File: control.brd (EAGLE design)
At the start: 146.1 x 33.7 mm, 4 parts, among them J1 1-2328702-0, U2 ESP32-DEVKITC-32D

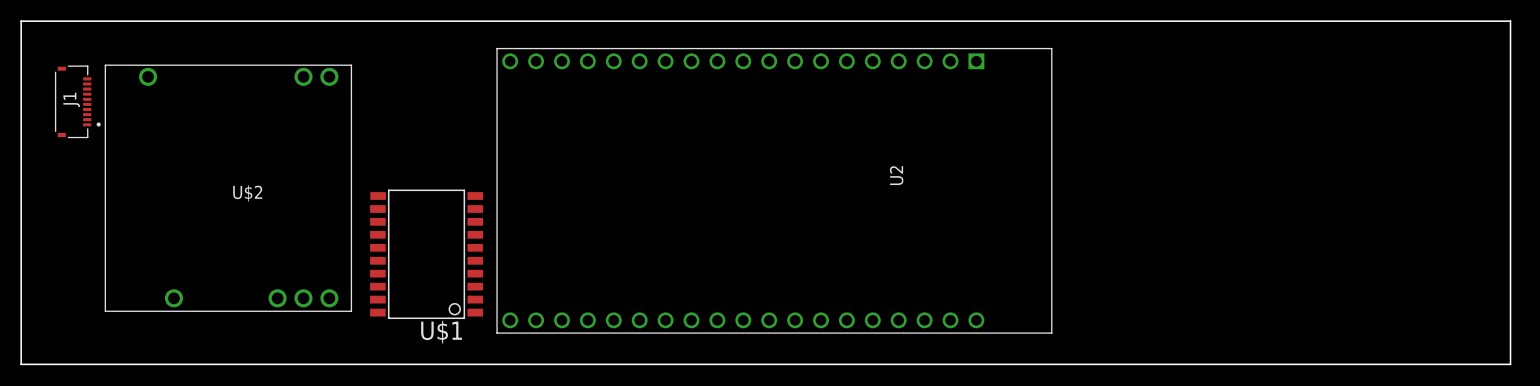
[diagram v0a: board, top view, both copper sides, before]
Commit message: lamp board finished, working on control
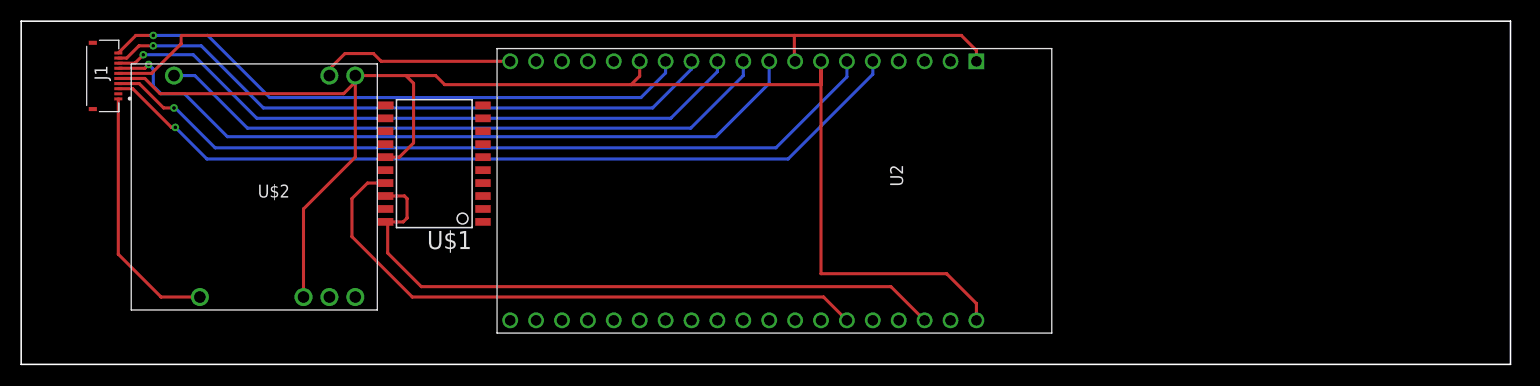
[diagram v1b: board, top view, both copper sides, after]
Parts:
- moved U$1 8.92 mm to (40.5, 19.7)
- moved J1 3.97 mm to (9.53, 26.0)
- moved U$2 2.54 mm to (34.9, 29.5)
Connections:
- removed net EXT_5V: U2.19
- removed net GND1: U2.14
- removed net GND3: U2.20
- new net 5V: U$2.VIN, U2.19
- new net BL: J1.8, U2.11
- new net CLK: J1.4, U2.6
- new net EN: U$2.ENABLE, U2.10
- new net GND: J1.5, U$1.GND, U$2.GND@1, U$2.GND@2, U2.14, U2.20, U2.7
- new net HV: J1.1, U$2.VOUT
- new net IN: J1.9, U2.12
- new net LE: J1.7, U2.9
- new net OUT: J1.10, U2.13
- new net POL: J1.3, U2.5
- new net SCL: U$1.SCL@0, U$1.SCL@1, U2.22
- new net SDA: U$1.SDA, U2.25
- net 3V3: now also J1.6, U2.8
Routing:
- net GND: track 0.00 -> 148.3 mm
- net 3V3: track 0.00 -> 90.4 mm
- net POL: track 0.00 -> 81.6 mm, vias 0 -> 1
- net CLK: track 0.00 -> 78.5 mm, vias 0 -> 1
- net LE: track 0.00 -> 72.2 mm, vias 0 -> 1
- net SCL: track 0.00 -> 64.8 mm
- net BL: track 0.00 -> 64.6 mm, vias 0 -> 1
- net IN: track 0.00 -> 61.6 mm, vias 0 -> 1
- net EN: track 0.00 -> 61.5 mm
- net SDA: track 0.00 -> 59.6 mm
- net OUT: track 0.00 -> 59.1 mm, vias 0 -> 1
- net HV: track 0.00 -> 25.0 mm
- net 5V: track 0.00 -> 19.3 mm

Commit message: add readme, brushup board
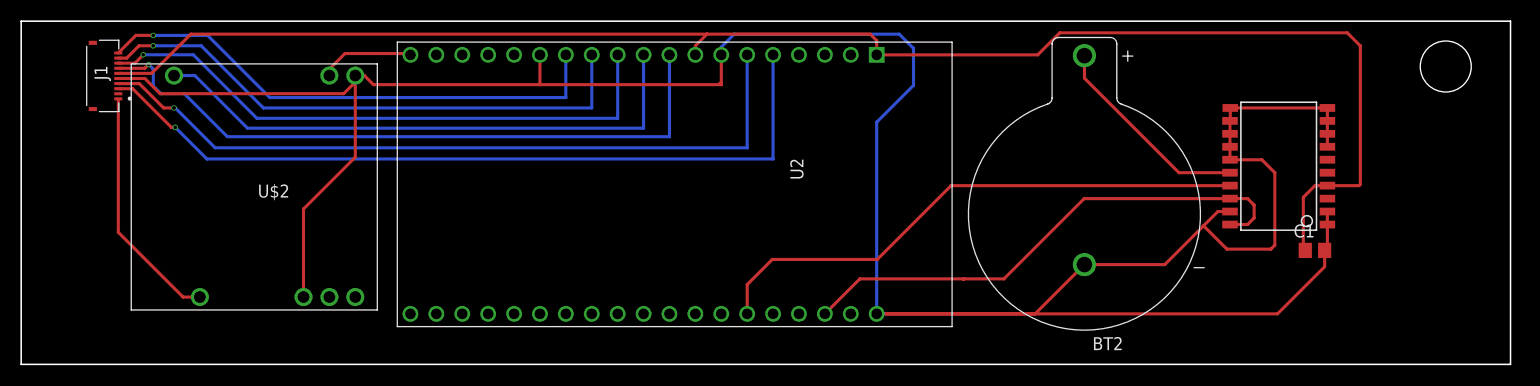
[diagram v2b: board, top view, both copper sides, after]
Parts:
- added BT2: 103, 103:BAT_103
- added C1: (no value), rcl:C0805
- moved U$1 82.8 mm to (123.3, 19.4)
- moved U2 9.80 mm to (64.1, 17.7)
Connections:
- removed net GND2: U2.26
- new net BAT: BT2.P, U$1.V_{BAT}
- net 3V3: now also C1.2, U$1.VCC
- net GND: now also BT2.N, C1.1, U$1.N.C.-0, U$1.N.C.-1, U$1.N.C.-10, U$1.N.C.-2, U$1.N.C.-3, U$1.N.C.-4, U$1.N.C.-5, U$1.N.C.-6, U$1.N.C.-7, U$1.N.C.-8, U$1.N.C.-9, U2.26
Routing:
- net GND: track 148.3 -> 267.5 mm
- net 3V3: track 90.4 -> 153.9 mm
- net BAT: track 0.00 -> 20.3 mm
- net SCL: track 64.8 -> 51.0 mm
- net 5V: track 19.3 -> 9.27 mm
- net OUT: track 59.1 -> 51.3 mm
- net IN: track 61.6 -> 54.7 mm
- net BL: track 64.6 -> 58.1 mm
- net EN: track 61.5 -> 55.4 mm
- net LE: track 72.2 -> 66.1 mm
- net SDA: track 59.6 -> 54.2 mm
- net CLK: track 78.5 -> 73.4 mm
- net POL: track 81.6 -> 77.3 mm
- net HV: track 25.0 -> 23.7 mm

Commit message: added potentio, readme update
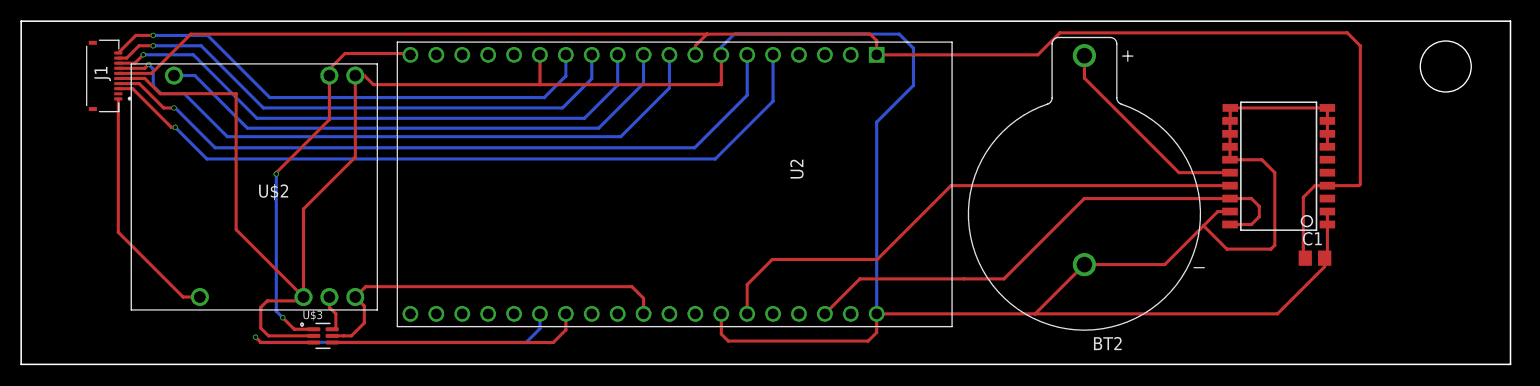
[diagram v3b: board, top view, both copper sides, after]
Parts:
- added U$3: MAX5461EXT+T, MAX5461EXT_T:SOT65P210X110-6N
- moved C1 0.76 mm to (126.9, 10.4), turned to 0 degrees
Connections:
- new net CS: U$3.4, U2.32
- new net RADJ: U$2.RADJUST, U$3.6
- new net UD: U$3.3, U2.33
- new net VADJ: U$2.VBIAS, U$3.5, U2.29
- net 3V3: now also C1.1; no longer C1.2
- net 5V: now also U$3.1
- net GND: now also C1.2, U$3.2; no longer C1.1
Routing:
- net VADJ: track 0.00 -> 37.3 mm
- net UD: track 0.00 -> 36.0 mm, vias 0 -> 1
- net 5V: track 9.27 -> 38.9 mm, vias 0 -> 2
- net GND: track 267.5 -> 294.3 mm
- net CS: track 0.00 -> 25.0 mm
- net RADJ: track 0.00 -> 3.72 mm
- net POL: track 77.3 -> 74.0 mm
- net CLK: track 73.4 -> 70.4 mm
- net LE: track 66.1 -> 63.3 mm
- net EN: track 55.4 -> 52.8 mm
- net BL: track 58.1 -> 56.2 mm
- net IN: track 54.7 -> 53.0 mm
- net OUT: track 51.3 -> 50.1 mm
- net SCL: track 51.0 -> 51.8 mm
- net 3V3: track 153.9 -> 154.7 mm

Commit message: reg update
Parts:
- added C2: 0.1u, rcl:C0805
- added C3, C4, C5: 100u, rcl:C1210
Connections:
- net 5V: now also C2.1, C3.2, C4.2, C5.2
- net GND: now also C2.2, C3.1, C4.1, C5.1
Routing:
- net GND: track 294.3 -> 337.7 mm, vias 0 -> 2
- net 5V: track 38.9 -> 78.8 mm, vias 2 -> 4
- net UD: track 36.0 -> 28.3 mm
- net HV: track 23.7 -> 22.7 mm
- net POL: track 74.0 -> 73.2 mm

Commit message: Found wurth typec
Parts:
- added J2: 12401598E4#2A, 12401598E4_2A:AMPHENOL_12401598E4#2A
- added R1, R2: 2k2, rcl:R0805
- moved C4 3.14 mm to (4.70, 15.0)
- moved C3 3.14 mm to (4.70, 20.3)
- moved C5 3.14 mm to (4.70, 9.65)
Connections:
- new net RST: U$1.!RST, U2.30
- new net SHIELD: J2.SH1, J2.SH2, J2.SH3, J2.SH4
- new net VBUS: J2.A4, J2.A9, J2.B4, J2.B9
- net 3V3: now also R1.2, R2.2
- net GND: now also J2.A1, J2.A12, J2.B1, J2.B12
- net SCL: now also R2.1
- net SDA: now also R1.1
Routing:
- net RST: track 0.00 -> 81.9 mm, vias 0 -> 1
- net 3V3: track 154.7 -> 182.3 mm, vias 0 -> 2
- net SDA: track 54.2 -> 59.9 mm
- net 5V: track 78.8 -> 81.2 mm
- net SCL: track 51.8 -> 53.1 mm
- net GND: track 337.7 -> 338.6 mm
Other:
- outline, holes or cut-outs redrawn

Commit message: started ratsnest, finished usb-c viring
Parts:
- added R3, R4: 5k1, rcl:R0805
- added X1: 22-23-2021, con-molex:22-23-2021
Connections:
- removed net VBUS: J2.A4, J2.A9, J2.B4, J2.B9
- new net DN: J2.A7, J2.B7, X1.1
- new net DP: J2.A6, J2.B6, X1.2
- new net N$1: J2.B5, R3.2
- new net N$2: J2.A5, R4.2
- net 5V: now also J2.A4, J2.A9, J2.B4, J2.B9
- net GND: now also R3.1, R4.1
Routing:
- net 5V: track 81.2 -> 198.0 mm, vias 4 -> 8
- net GND: track 338.6 -> 364.6 mm
- net SHIELD: track 0.00 -> 21.6 mm
- net DN: track 0.00 -> 19.0 mm, vias 0 -> 3
- net DP: track 0.00 -> 14.5 mm, vias 0 -> 1
- net N$1: track 0.00 -> 14.3 mm, vias 0 -> 2
- net 3V3: track 182.3 -> 174.9 mm
- net N$2: track 0.00 -> 3.97 mm
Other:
- outline, holes or cut-outs redrawn
